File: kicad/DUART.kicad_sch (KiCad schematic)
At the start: 5 parts, among them J2 Conn_01x20_Pin, U11 68681, Y1 Crystal

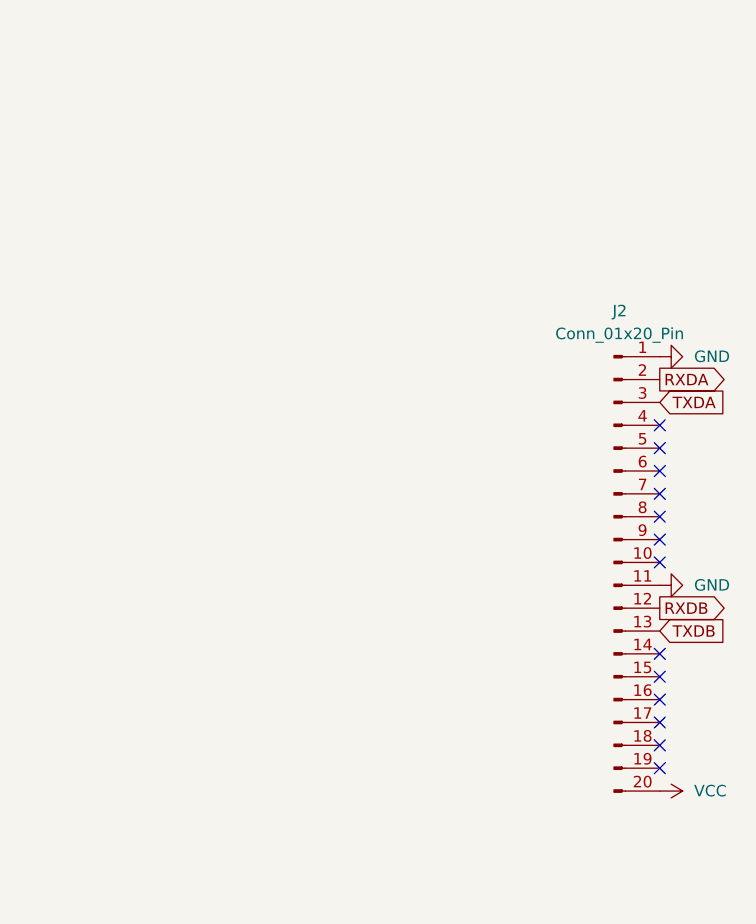
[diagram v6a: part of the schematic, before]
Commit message: Added Bus error handling
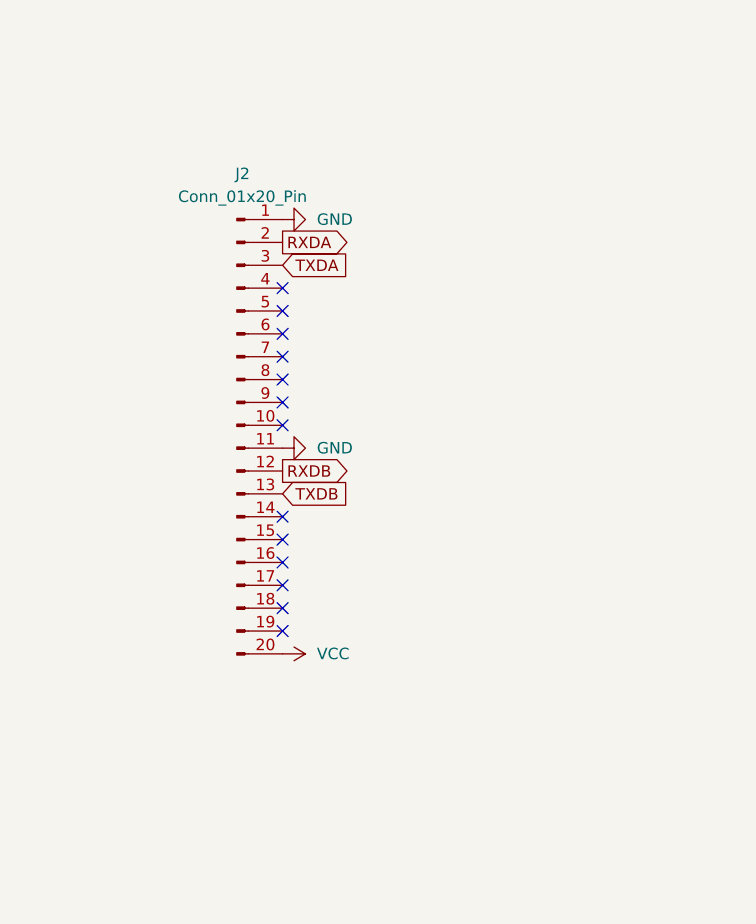
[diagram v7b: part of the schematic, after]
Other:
- moved on the sheet: J2
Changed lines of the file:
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@@
   (junction (at 104.14 44.45) (diameter 0) (color 0 0 0 0)
   )
-  (no_connect (at 254 120.65))
-  (no_connect (at 254 113.03))
-  (no_connect (at 254 87.63))
-  (no_connect (at 254 92.71))
-  (no_connect (at 254 82.55))
-  (no_connect (at 254 97.79))
-  (no_connect (at 254 118.11))
-  (no_connect (at 254 110.49))
-  (no_connect (at 254 90.17))
+  (no_connect (at 212.09 105.41))
+  (no_connect (at 212.09 97.79))
+  (no_connect (at 212.09 72.39))
+  (no_connect (at 212.09 77.47))
+  (no_connect (at 212.09 67.31))
+  (no_connect (at 212.09 82.55))
+  (no_connect (at 212.09 102.87))
+  (no_connect (at 212.09 95.25))
+  (no_connect (at 212.09 74.93))
   (no_connect (at 167.64 106.68))
   (no_connect (at 167.64 104.14))
@@
   (no_connect (at 167.64 96.52))
   (no_connect (at 167.64 99.06))
-  (no_connect (at 254 107.95))
-  (no_connect (at 254 115.57))
-  (no_connect (at 254 85.09))
-  (no_connect (at 254 95.25))
+  (no_connect (at 212.09 92.71))
+  (no_connect (at 212.09 100.33))
+  (no_connect (at 212.09 69.85))
+  (no_connect (at 212.09 80.01))
   (bus_entry (at 92.71 83.82) (size 2.54 -2.54)
     (stroke (width 0) (type default))
@@
     )
   )
-  (global_label "TXDB" (shape input) (at 254 105.41 0) (fields_autoplaced)
-    (effects (font (size 1.27 1.27)) (justify left))
-    (property "Intersheetrefs" "${INTERSHEET_REFS}" (at 261.6229 105.41 0)
+  (global_label "TXDB" (shape input) (at 212.09 90.17 0) (fields_autoplaced)
+    (effects (font (size 1.27 1.27)) (justify left))
+    (property "Intersheetrefs" "${INTERSHEET_REFS}" (at 219.7129 90.17 0)
       (effects (font (size 1.27 1.27)) (justify left) hide)
     )
@@
     )
   )
-  (global_label "TXDA" (shape input) (at 254 80.01 0) (fields_autoplaced)
-    (effects (font (size 1.27 1.27)) (justify left))
-    (property "Intersheetrefs" "${INTERSHEET_REFS}" (at 260.9488 79.9306 0)
+  (global_label "TXDA" (shape input) (at 212.09 64.77 0) (fields_autoplaced)
+    (effects (font (size 1.27 1.27)) (justify left))
+    (property "Intersheetrefs" "${INTERSHEET_REFS}" (at 219.0388 64.6906 0)
       (effects (font (size 1.27 1.27)) (justify left) hide)
     )
@@
     )
   )
-  (global_label "RXDA" (shape output) (at 254 77.47 0) (fields_autoplaced)
-    (effects (font (size 1.27 1.27)) (justify left))
-    (property "Intersheetrefs" "${INTERSHEET_REFS}" (at 261.2512 77.3906 0)
-      (effects (font (size 1.27 1.27)) (justify left) hide)
-    )
-  )
-  (global_label "RXDB" (shape output) (at 254 102.87 0) (fields_autoplaced)
-    (effects (font (size 1.27 1.27)) (justify left))
-    (property "Intersheetrefs" "${INTERSHEET_REFS}" (at 261.9253 102.87 0)
+  (global_label "RXDA" (shape output) (at 212.09 62.23 0) (fields_autoplaced)
+    (effects (font (size 1.27 1.27)) (justify left))
+    (property "Intersheetrefs" "${INTERSHEET_REFS}" (at 219.3412 62.1506 0)
+      (effects (font (size 1.27 1.27)) (justify left) hide)
+    )
+  )
+  (global_label "RXDB" (shape output) (at 212.09 87.63 0) (fields_autoplaced)
+    (effects (font (size 1.27 1.27)) (justify left))
+    (property "Intersheetrefs" "${INTERSHEET_REFS}" (at 220.0153 87.63 0)
       (effects (font (size 1.27 1.27)) (justify left) hide)
     )
@@
     )
   )
-  (symbol (lib_id "power:VCC") (at 254 123.19 270) (unit 1)
-    (in_bom yes) (on_board yes) (dnp no) (fields_autoplaced)
-    (property "Reference" "#PWR032" (at 250.19 123.19 0)
-      (effects (font (size 1.27 1.27)) hide)
-    )
-    (property "Value" "VCC" (at 257.81 123.19 90)
+  (symbol (lib_id "power:VCC") (at 212.09 107.95 270) (unit 1)
+    (in_bom yes) (on_board yes) (dnp no) (fields_autoplaced)
+    (property "Reference" "#PWR032" (at 208.28 107.95 0)
+      (effects (font (size 1.27 1.27)) hide)
+    )
+    (property "Value" "VCC" (at 215.9 107.95 90)
       (effects (font (size 1.27 1.27)) (justify left))
     )
-    (property "Footprint" "" (at 254 123.19 0)
-      (effects (font (size 1.27 1.27)) hide)
-    )
-    (property "Datasheet" "" (at 254 123.19 0)
+    (property "Footprint" "" (at 212.09 107.95 0)
+      (effects (font (size 1.27 1.27)) hide)
+    )
+    (property "Datasheet" "" (at 212.09 107.95 0)
       (effects (font (size 1.27 1.27)) hide)
     )
@@
     )
   )
-  (symbol (lib_id "Connector:Conn_01x20_Pin") (at 248.92 97.79 0) (unit 1)
-    (in_bom yes) (on_board yes) (dnp no) (fields_autoplaced)
-    (property "Reference" "J2" (at 249.555 69.85 0)
+  (symbol (lib_id "Connector:Conn_01x20_Pin") (at 207.01 82.55 0) (unit 1)
+    (in_bom yes) (on_board yes) (dnp no) (fields_autoplaced)
+    (property "Reference" "J2" (at 207.645 54.61 0)
       (effects (font (size 1.27 1.27)))
     )
-    (property "Value" "Conn_01x20_Pin" (at 249.555 72.39 0)
+    (property "Value" "Conn_01x20_Pin" (at 207.645 57.15 0)
       (effects (font (size 1.27 1.27)))
     )
-    (property "Footprint" "" (at 248.92 97.79 0)
-      (effects (font (size 1.27 1.27)) hide)
-    )
-    (property "Datasheet" "~" (at 248.92 97.79 0)
+    (property "Footprint" "" (at 207.01 82.55 0)
+      (effects (font (size 1.27 1.27)) hide)
+    )
+    (property "Datasheet" "~" (at 207.01 82.55 0)
       (effects (font (size 1.27 1.27)) hide)
     )
@@
     )
   )
-  (symbol (lib_id "power:GND") (at 254 74.93 90) (unit 1)
-    (in_bom yes) (on_board yes) (dnp no) (fields_autoplaced)
-    (property "Reference" "#PWR031" (at 260.35 74.93 0)
-      (effects (font (size 1.27 1.27)) hide)
-    )
-    (property "Value" "GND" (at 257.81 74.9299 90)
+  (symbol (lib_id "power:GND") (at 212.09 59.69 90) (unit 1)
+    (in_bom yes) (on_board yes) (dnp no) (fields_autoplaced)
+    (property "Reference" "#PWR031" (at 218.44 59.69 0)
+      (effects (font (size 1.27 1.27)) hide)
+    )
+    (property "Value" "GND" (at 215.9 59.6899 90)
       (effects (font (size 1.27 1.27)) (justify right))
     )
-    (property "Footprint" "" (at 254 74.93 0)
-      (effects (font (size 1.27 1.27)) hide)
-    )
-    (property "Datasheet" "" (at 254 74.93 0)
+    (property "Footprint" "" (at 212.09 59.69 0)
+      (effects (font (size 1.27 1.27)) hide)
+    )
+    (property "Datasheet" "" (at 212.09 59.69 0)
       (effects (font (size 1.27 1.27)) hide)
     )
@@
     )
   )
-  (symbol (lib_id "power:GND") (at 254 100.33 90) (unit 1)
-    (in_bom yes) (on_board yes) (dnp no) (fields_autoplaced)
-    (property "Reference" "#PWR033" (at 260.35 100.33 0)
-      (effects (font (size 1.27 1.27)) hide)
-    )
-    (property "Value" "GND" (at 257.81 100.3299 90)
+  (symbol (lib_id "power:GND") (at 212.09 85.09 90) (unit 1)
+    (in_bom yes) (on_board yes) (dnp no) (fields_autoplaced)
+    (property "Reference" "#PWR033" (at 218.44 85.09 0)
+      (effects (font (size 1.27 1.27)) hide)
+    )
+    (property "Value" "GND" (at 215.9 85.0899 90)
       (effects (font (size 1.27 1.27)) (justify right))
     )
-    (property "Footprint" "" (at 254 100.33 0)
-      (effects (font (size 1.27 1.27)) hide)
-    )
-    (property "Datasheet" "" (at 254 100.33 0)
-      (effects (font (size 1.27 1.27)) hide)
-    )
+    (property "Footprint" "" (at 212.09 85.09 0)
+      (effects (font (size 1.27 1.27)) hide)
+    )
+    (property "Datasheet" "" (at 212.09 85.09 0)
+      (effects (font (size 1.27 1.27)) hide)
+    )

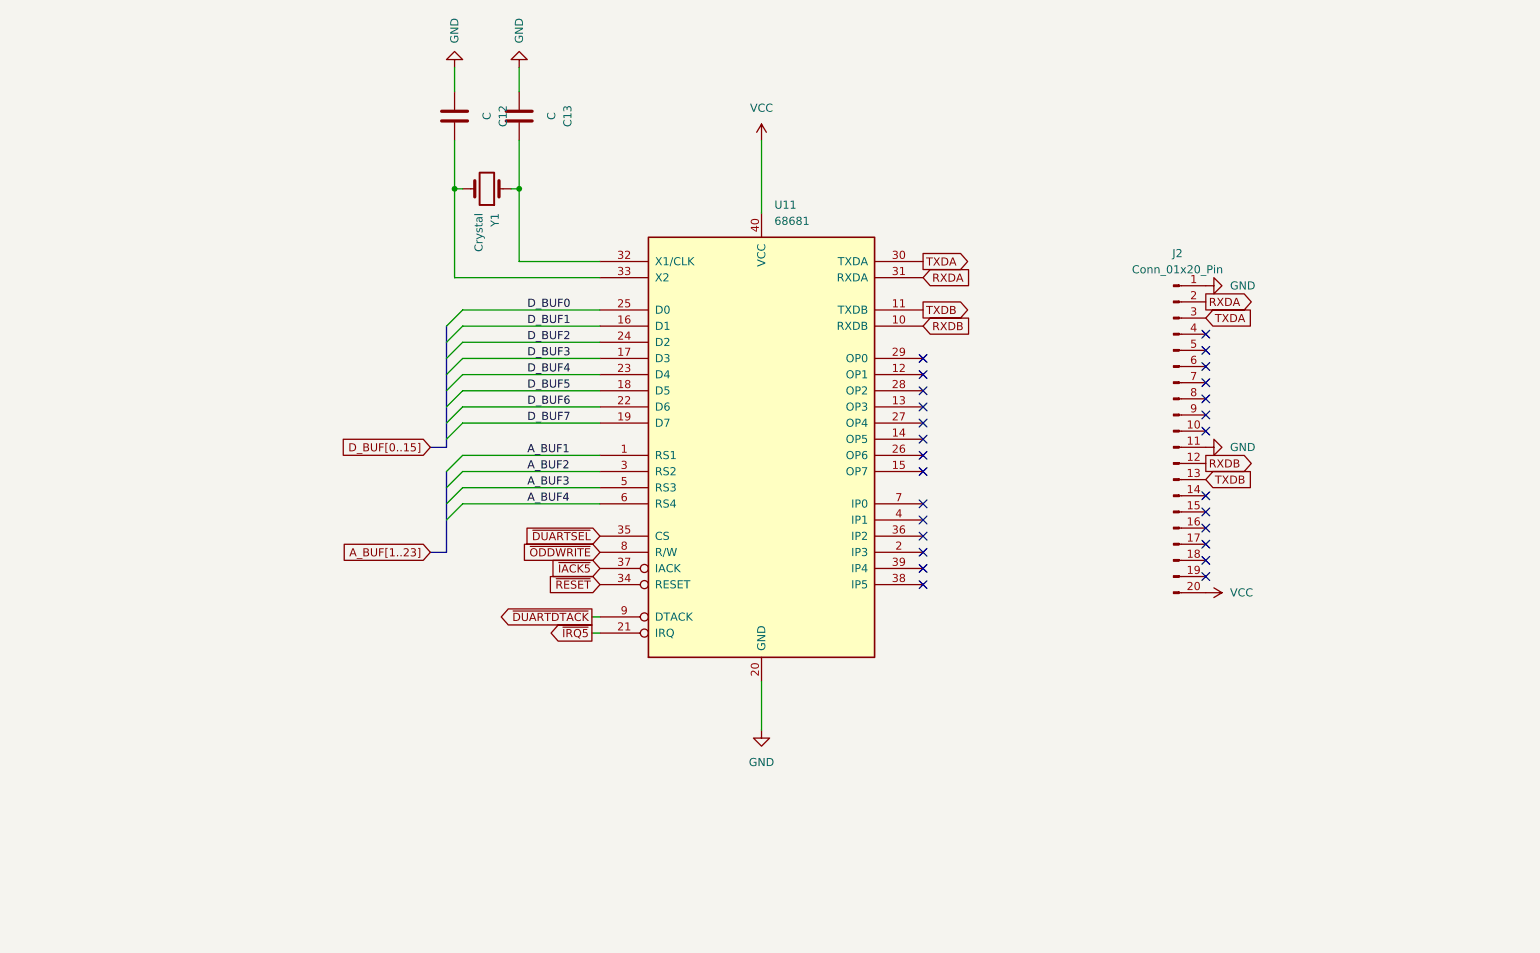
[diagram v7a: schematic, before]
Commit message: switched to GALasm
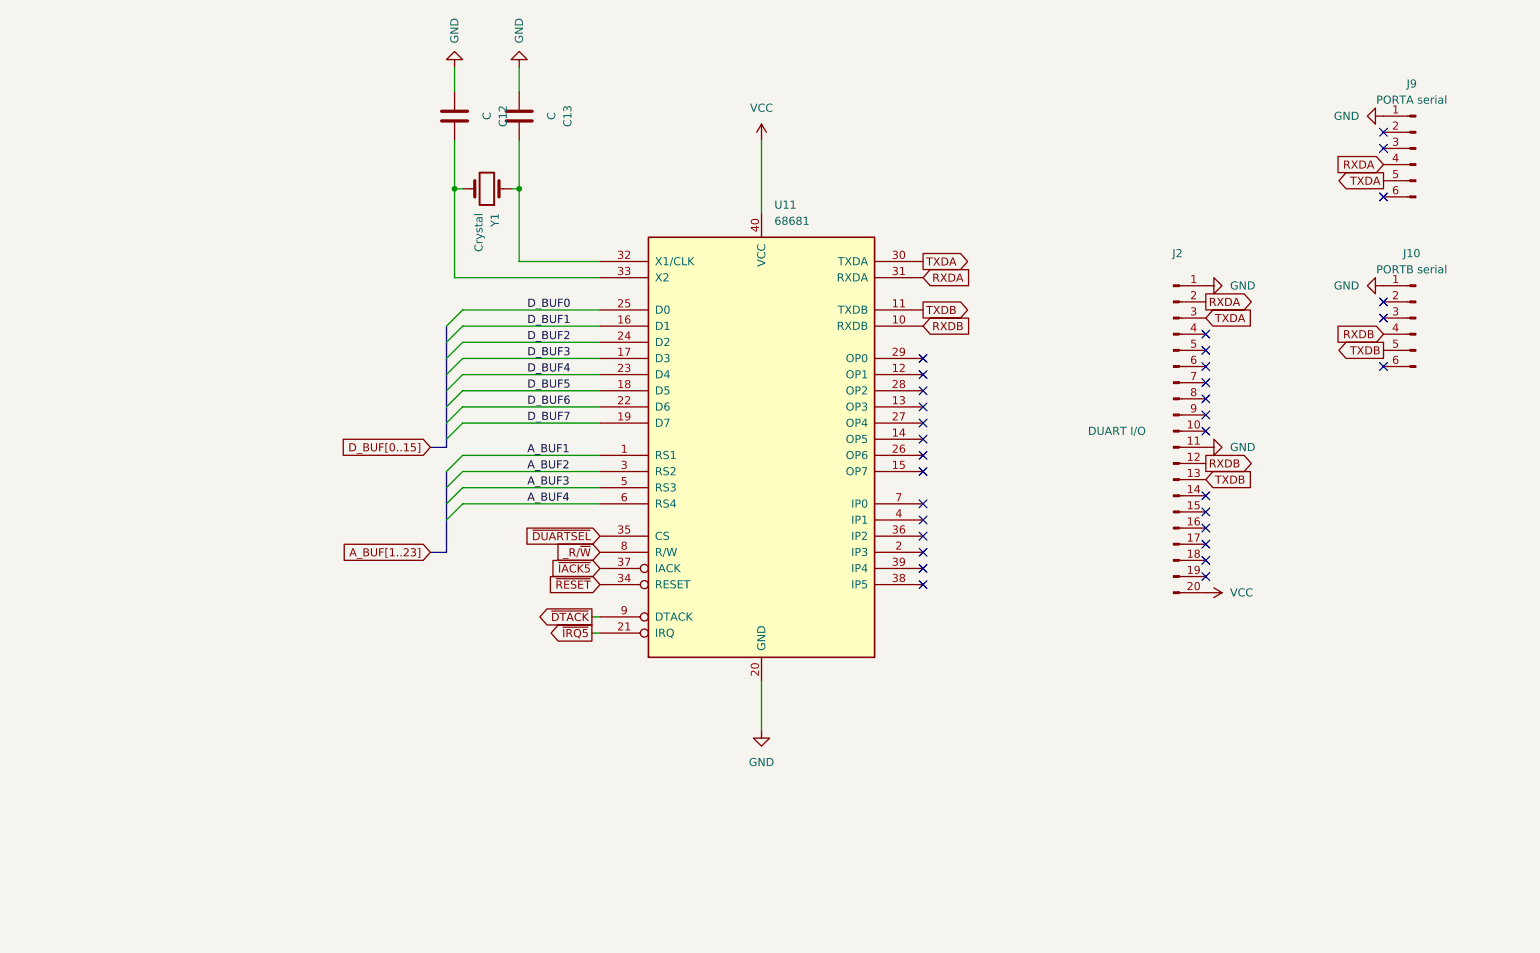
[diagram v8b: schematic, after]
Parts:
- added J10: PORTB serial, symbol Connector:Conn_01x06_Pin
- added J9: PORTA serial, symbol Connector:Conn_01x06_Pin
- J2: value Conn_01x20_Pin -> DUART I/O
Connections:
- net GND: now also J10.1 (Pin_1), J9.1 (Pin_1)
- net RXDA: now also J9.4 (Pin_4)
- net RXDB: now also J10.4 (Pin_4)
- net TXDA: now also J9.5 (Pin_5)
- net TXDB: now also J10.5 (Pin_5)
- net ~{DUARTDTACK} renamed ~{DTACK}
- net ~{ODDWRITE} renamed _R/~{W}
- no-connect marks 27 -> 33
